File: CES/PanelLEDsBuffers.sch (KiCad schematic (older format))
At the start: 67 parts

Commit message: ExpansionConnectors
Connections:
- net at J?.1 (Pin_1): now also U?.6; no longer U?.12
- net at J?.10 (Pin_10): now also U?.12; no longer U?.6
- net at J?.11 (Pin_11): now also U?.2; no longer U?.4
- net at J?.12 (Pin_12): now also U?.4; no longer U?.2
- net at J?.13 (Pin_13): now also U?.6; no longer U?.12
- net at J?.14 (Pin_14): now also U?.8; no longer U?.10
- net at J?.15 (Pin_15): now also U?.10; no longer U?.8
- net at J?.16 (Pin_16): now also U?.12; no longer U?.6
- net at J?.2 (Pin_2): now also U?.8; no longer U?.10
- net at J?.3 (Pin_3): now also U?.10; no longer U?.8
- net at J?.4 (Pin_4): now also U?.12; no longer U?.6
- net at J?.5 (Pin_5): now also U?.2; no longer U?.4
- net at J?.6 (Pin_6): now also U?.4; no longer U?.2
- net at J?.7 (Pin_7): now also U?.6; no longer U?.12
- net at J?.8 (Pin_8): now also U?.8; no longer U?.10
- net at J?.9 (Pin_9): now also U?.10; no longer U?.8
- net at J?.1 (Pin_1): now also U?.10; no longer U?.4
- net at J?.10 (Pin_10): now also U?.4; no longer U?.10
- net at J?.11 (Pin_11): now also U?.6; no longer U?.8
- net at J?.12 (Pin_12): now also U?.8; no longer U?.6
- net at J?.13 (Pin_13): now also U?.10; no longer U?.4
- net at J?.14 (Pin_14): now also U?.12; no longer U?.2
- net at J?.15 (Pin_15): now also U?.2; no longer U?.12
- net at J?.16 (Pin_16): now also U?.4; no longer U?.10
- net at J?.2 (Pin_2): now also U?.12; no longer U?.2
- net at J?.3 (Pin_3): now also U?.2; no longer U?.12
- net at J?.4 (Pin_4): now also U?.4; no longer U?.10
- net at J?.5 (Pin_5): now also U?.6; no longer U?.8
- net at J?.6 (Pin_6): now also U?.8; no longer U?.6
- net at J?.7 (Pin_7): now also U?.10; no longer U?.4
- net at J?.8 (Pin_8): now also U?.12; no longer U?.2
- net at J?.9 (Pin_9): now also U?.2; no longer U?.12
- net at J?.1 (Pin_1): now also U?.2; no longer U?.8
- net at J?.10 (Pin_10): now also U?.8; no longer U?.2
- net at J?.11 (Pin_11): now also U?.10; no longer U?.12
- net at J?.12 (Pin_12): now also U?.12; no longer U?.10
- net at J?.13 (Pin_13): now also U?.2; no longer U?.8
- net at J?.14 (Pin_14): now also U?.4; no longer U?.6
- net at J?.15 (Pin_15): now also U?.6; no longer U?.4
- net at J?.16 (Pin_16): now also U?.8; no longer U?.2
- net at J?.2 (Pin_2): now also U?.4; no longer U?.6
- net at J?.3 (Pin_3): now also U?.6; no longer U?.4
- net at J?.4 (Pin_4): now also U?.8; no longer U?.2
- net at J?.5 (Pin_5): now also U?.10; no longer U?.12
- net at J?.6 (Pin_6): now also U?.12; no longer U?.10
- net at J?.7 (Pin_7): now also U?.2; no longer U?.8
- net at J?.8 (Pin_8): now also U?.4; no longer U?.6
- net at J?.9 (Pin_9): now also U?.6; no longer U?.4
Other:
- note removed: "TODO: Find a \nbetter connector"
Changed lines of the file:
@@
 $Descr A4 11693 8268
 encoding utf-8
-Sheet 12 15
+Sheet 12 16
 Title "CES"
 Date "2021-04-24"
@@
 L Connector:Conn_01x16_Male J?
 U 1 1 60C2ED9D
-P 9250 3350
+P 9250 3250
 AR Path="/60832DB9/60C2ED9D" Ref="J?"  Part="1"
 AR Path="/60832DB9/60BC5CB5/60C2ED9D" Ref="J?"  Part="1"
-F 0 "J?" H 9350 2400 50  0000 R CNN
-F 1 "PanelEnd" H 9450 4150 50  0000 R CNN
-F 2 "" H 9250 3350 50  0001 C CNN
-F 3 "~" H 9250 3350 50  0001 C CNN
-	1    9250 3350
-	-1   0    0    1
+F 0 "J?" H 9350 2300 50  0000 R CNN
+F 1 "PanelEnd" H 9450 4050 50  0000 R CNN
+F 2 "" H 9250 3250 50  0001 C CNN
+F 3 "~" H 9250 3250 50  0001 C CNN
+	1    9250 3250
+	-1   0    0    -1
 $EndComp
 Wire Wire Line
@@
 L Connector:Conn_01x16_Male J?
 U 1 1 60C2EDF1
-P 6750 3350
+P 6750 3250
 AR Path="/60832DB9/60C2EDF1" Ref="J?"  Part="1"
 AR Path="/60832DB9/60BC5CB5/60C2EDF1" Ref="J?"  Part="1"
-F 0 "J?" H 6850 2400 50  0000 R CNN
-F 1 "PanelMem" H 6950 4150 50  0000 R CNN
-F 2 "" H 6750 3350 50  0001 C CNN
-F 3 "~" H 6750 3350 50  0001 C CNN
-	1    6750 3350
-	-1   0    0    1
+F 0 "J?" H 6850 2300 50  0000 R CNN
+F 1 "PanelMem" H 6950 4050 50  0000 R CNN
+F 2 "" H 6750 3250 50  0001 C CNN
+F 3 "~" H 6750 3250 50  0001 C CNN
+	1    6750 3250
+	-1   0    0    -1
 $EndComp
 Wire Wire Line
@@
 Text GLabel 4950 1150 0    50   Input ~ 0
 VDB1
-Text Notes 9000 4400 0    50   ~ 0
-TODO: Find a \nbetter connector
 Wire Wire Line
 	4950 800  5150 800
@@
 L Connector:Conn_01x16_Male J?
 U 1 1 60C2EE48
-P 4450 3350
+P 4450 3250
 AR Path="/60832DB9/60C2EE48" Ref="J?"  Part="1"
 AR Path="/60832DB9/60BC5CB5/60C2EE48" Ref="J?"  Part="1"
-F 0 "J?" H 4550 2400 50  0000 R CNN
-F 1 "PanelRT" H 4650 4150 50  0000 R CNN
-F 2 "" H 4450 3350 50  0001 C CNN
-F 3 "~" H 4450 3350 50  0001 C CNN
-	1    4450 3350
-	-1   0    0    1
+F 0 "J?" H 4550 2300 50  0000 R CNN
+F 1 "PanelRT" H 4650 4050 50  0000 R CNN
+F 2 "" H 4450 3250 50  0001 C CNN
+F 3 "~" H 4450 3250 50  0001 C CNN
+	1    4450 3250
+	-1   0    0    -1
 $EndComp
 Wire Wire Line

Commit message: Control Unit
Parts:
- gave numbers to parts that had none: 19

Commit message: Assigning footprints and generating netlist
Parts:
- C1301, C1302, C1303, C1304, C1305, C1306, C1307, C1308: footprint (none) -> Capacitor_THT:CP_Radial_D5.0mm_P2.50mm
- J1301, J1302, J1303: footprint (none) -> Connector_PinHeader_2.54mm:PinHeader_1x16_P2.54mm_Vertical
- U1301, U1302, U1303, U1304, U1305, U1306, U1307, U1308: footprint (none) -> Package_DIP:DIP-14_W7.62mm

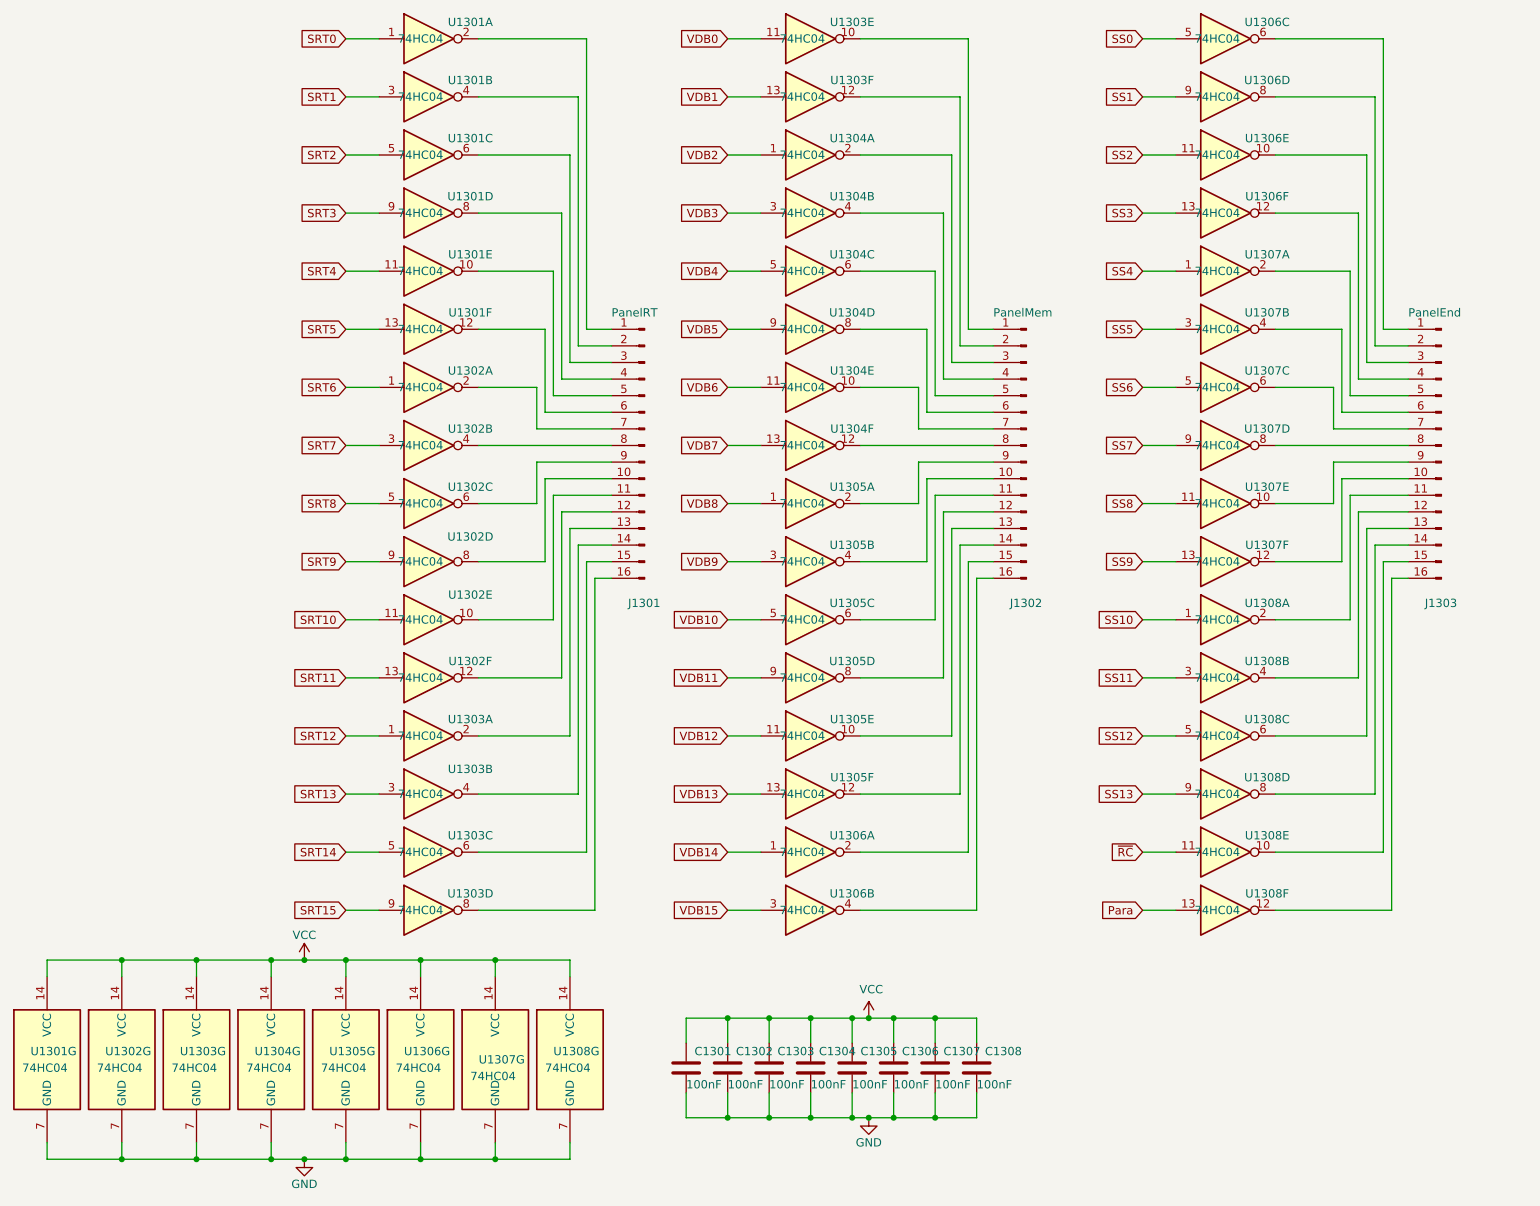
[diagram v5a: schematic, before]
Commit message: Correcting footprints errors
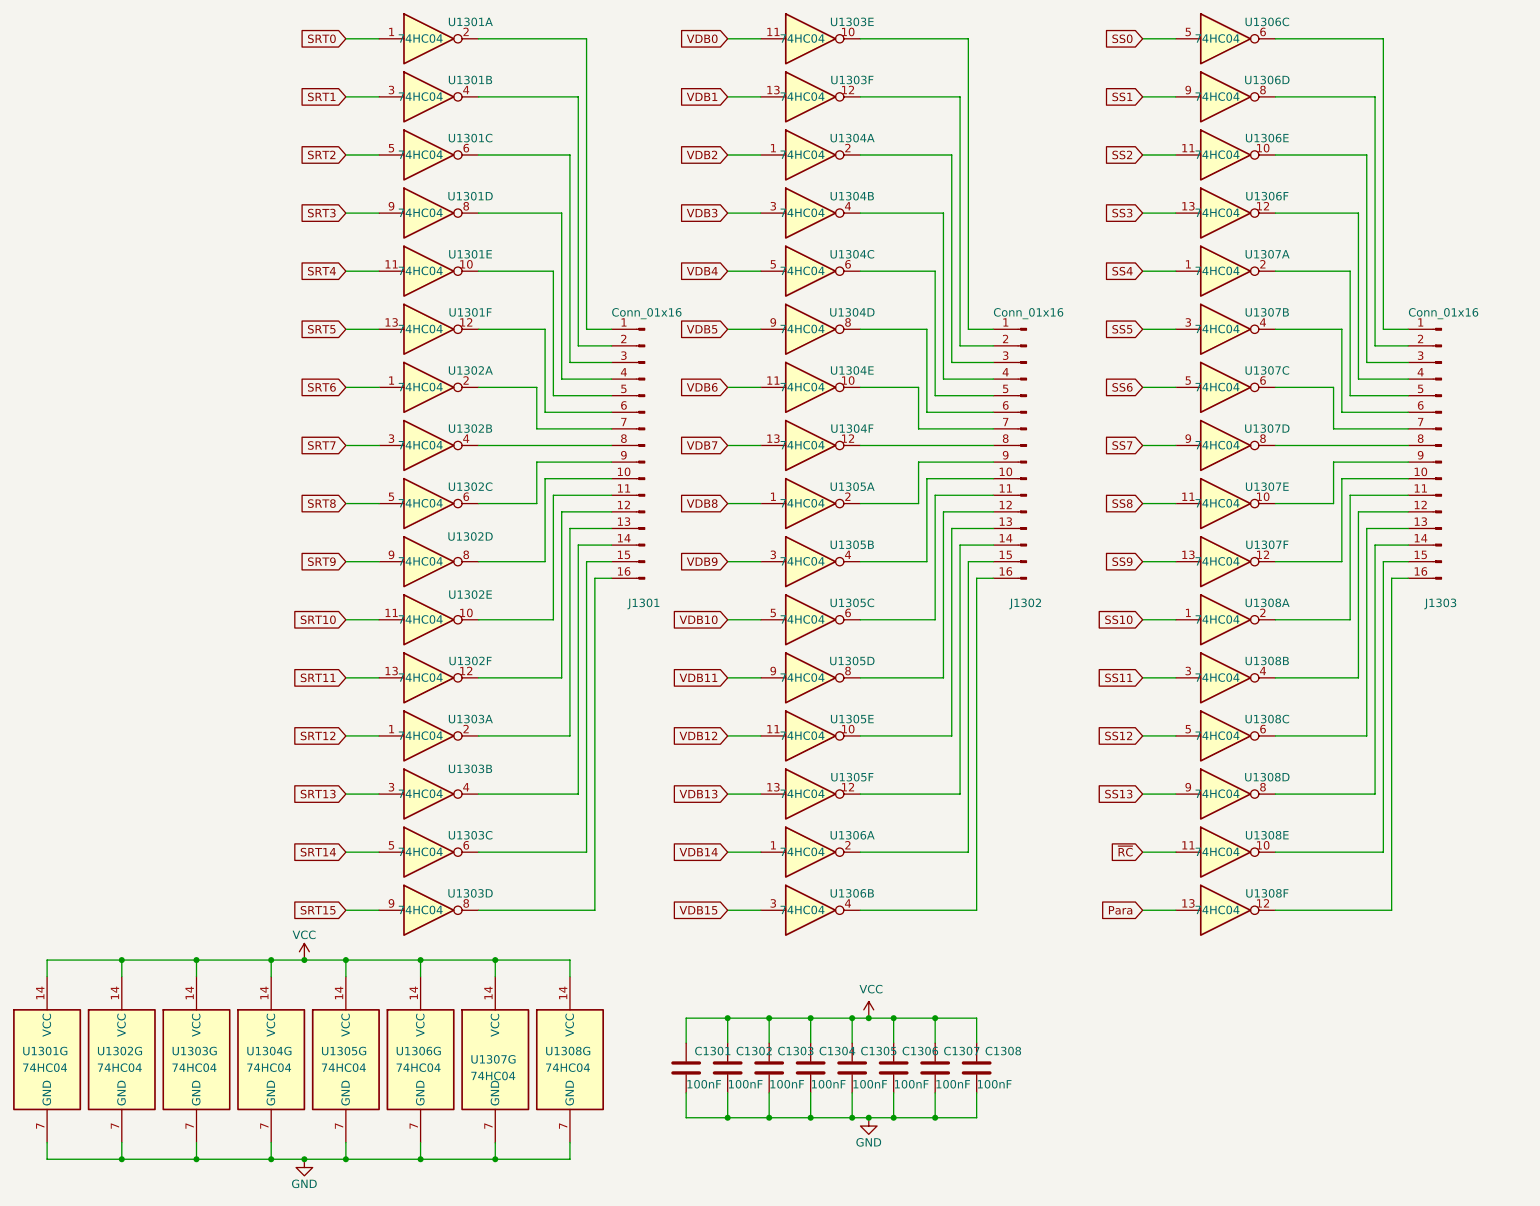
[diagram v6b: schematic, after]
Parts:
- C1301, C1302, C1303, C1304, C1305, C1306, C1307, C1308: footprint Capacitor_THT:CP_Radial_D5.0mm_P2.50mm -> Capacitor_THT:C_Disc_D4.3mm_W1.9mm_P5.00mm
- J1301: value PanelRT -> Conn_01x16
- J1302: value PanelMem -> Conn_01x16
- J1303: value PanelEnd -> Conn_01x16
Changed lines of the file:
@@
 AR Path="/60832DB9/60BC5CB5/60C2ED9D" Ref="J1303"  Part="1"
 F 0 "J1303" H 9350 2300 50  0000 R CNN
-F 1 "PanelEnd" H 9450 4050 50  0000 R CNN
+F 1 "Conn_01x16" H 9450 4050 50  0000 R CNN
 F 2 "Connector_PinHeader_2.54mm:PinHeader_1x16_P2.54mm_Vertical" H 9250 3250 50  0001 C CNN
 F 3 "~" H 9250 3250 50  0001 C CNN
@@
 AR Path="/60832DB9/60BC5CB5/60C2EDF1" Ref="J1302"  Part="1"
 F 0 "J1302" H 6850 2300 50  0000 R CNN
-F 1 "PanelMem" H 6950 4050 50  0000 R CNN
+F 1 "Conn_01x16" H 6950 4050 50  0000 R CNN
 F 2 "Connector_PinHeader_2.54mm:PinHeader_1x16_P2.54mm_Vertical" H 6750 3250 50  0001 C CNN
 F 3 "~" H 6750 3250 50  0001 C CNN
@@
 AR Path="/60832DB9/60BC5CB5/60C2EE48" Ref="J1301"  Part="1"
 F 0 "J1301" H 4550 2300 50  0000 R CNN
-F 1 "PanelRT" H 4650 4050 50  0000 R CNN
+F 1 "Conn_01x16" H 4650 4050 50  0000 R CNN
 F 2 "Connector_PinHeader_2.54mm:PinHeader_1x16_P2.54mm_Vertical" H 4450 3250 50  0001 C CNN
 F 3 "~" H 4450 3250 50  0001 C CNN
@@
 U 7 1 60CD4AAA
 P 2650 6950
-F 0 "U1305" H 2550 7000 50  0000 L CNN
+F 0 "U1305" H 2500 7000 50  0000 L CNN
 F 1 "74HC04" H 2500 6900 50  0000 L CNN
 F 2 "Package_DIP:DIP-14_W7.62mm" H 2650 6950 50  0001 C CNN
@@
 U 7 1 60CD4AB0
 P 3100 6950
-F 0 "U1306" H 3000 7000 50  0000 L CNN
+F 0 "U1306" H 2950 7000 50  0000 L CNN
 F 1 "74HC04" H 2950 6900 50  0000 L CNN
 F 2 "Package_DIP:DIP-14_W7.62mm" H 3100 6950 50  0001 C CNN
@@
 U 7 1 60CD4AB6
 P 3550 6950
-F 0 "U1307" H 3450 6950 50  0000 L CNN
+F 0 "U1307" H 3400 6950 50  0000 L CNN
 F 1 "74HC04" H 3400 6850 50  0000 L CNN
 F 2 "Package_DIP:DIP-14_W7.62mm" H 3550 6950 50  0001 C CNN
@@
 U 7 1 60CD4ABC
 P 4000 6950
-F 0 "U1308" H 3900 7000 50  0000 L CNN
+F 0 "U1308" H 3850 7000 50  0000 L CNN
 F 1 "74HC04" H 3850 6900 50  0000 L CNN
 F 2 "Package_DIP:DIP-14_W7.62mm" H 4000 6950 50  0001 C CNN
@@
 U 7 1 60CD4AC2
 P 850 6950
-F 0 "U1301" H 750 7000 50  0000 L CNN
+F 0 "U1301" H 700 7000 50  0000 L CNN
 F 1 "74HC04" H 700 6900 50  0000 L CNN
 F 2 "Package_DIP:DIP-14_W7.62mm" H 850 6950 50  0001 C CNN
@@
 U 7 1 60CD4AC8
 P 1300 6950
-F 0 "U1302" H 1200 7000 50  0000 L CNN
+F 0 "U1302" H 1150 7000 50  0000 L CNN
 F 1 "74HC04" H 1150 6900 50  0000 L CNN
 F 2 "Package_DIP:DIP-14_W7.62mm" H 1300 6950 50  0001 C CNN
@@
 U 7 1 60CD4ACE
 P 1750 6950
-F 0 "U1303" H 1650 7000 50  0000 L CNN
+F 0 "U1303" H 1600 7000 50  0000 L CNN
 F 1 "74HC04" H 1600 6900 50  0000 L CNN
 F 2 "Package_DIP:DIP-14_W7.62mm" H 1750 6950 50  0001 C CNN
@@
 U 7 1 60CD4AD4
 P 2200 6950
-F 0 "U1304" H 2100 7000 50  0000 L CNN
+F 0 "U1304" H 2050 7000 50  0000 L CNN
 F 1 "74HC04" H 2050 6900 50  0000 L CNN
 F 2 "Package_DIP:DIP-14_W7.62mm" H 2200 6950 50  0001 C CNN
@@
 F 0 "C1307" H 6250 7100 50  0000 L CNN
 F 1 "100nF" H 6200 6900 50  0000 L CNN
-F 2 "Capacitor_THT:CP_Radial_D5.0mm_P2.50mm" H 6238 6850 50  0001 C CNN
+F 2 "Capacitor_THT:C_Disc_D4.3mm_W1.9mm_P5.00mm" H 6238 6850 50  0001 C CNN
 F 3 "~" H 6200 7000 50  0001 C CNN
 	1    6200 7000
@@
 F 0 "C1308" H 6500 7100 50  0000 L CNN
 F 1 "100nF" H 6450 6900 50  0000 L CNN
-F 2 "Capacitor_THT:CP_Radial_D5.0mm_P2.50mm" H 6488 6850 50  0001 C CNN
+F 2 "Capacitor_THT:C_Disc_D4.3mm_W1.9mm_P5.00mm" H 6488 6850 50  0001 C CNN
 F 3 "~" H 6450 7000 50  0001 C CNN
 	1    6450 7000
@@
 F 0 "C1306" H 6000 7100 50  0000 L CNN
 F 1 "100nF" H 5950 6900 50  0000 L CNN
-F 2 "Capacitor_THT:CP_Radial_D5.0mm_P2.50mm" H 5988 6850 50  0001 C CNN
+F 2 "Capacitor_THT:C_Disc_D4.3mm_W1.9mm_P5.00mm" H 5988 6850 50  0001 C CNN
 F 3 "~" H 5950 7000 50  0001 C CNN
 	1    5950 7000
@@
 F 0 "C1305" H 5750 7100 50  0000 L CNN
 F 1 "100nF" H 5700 6900 50  0000 L CNN
-F 2 "Capacitor_THT:CP_Radial_D5.0mm_P2.50mm" H 5738 6850 50  0001 C CNN
+F 2 "Capacitor_THT:C_Disc_D4.3mm_W1.9mm_P5.00mm" H 5738 6850 50  0001 C CNN
 F 3 "~" H 5700 7000 50  0001 C CNN
 	1    5700 7000
@@
 F 0 "C1304" H 5500 7100 50  0000 L CNN
 F 1 "100nF" H 5450 6900 50  0000 L CNN
-F 2 "Capacitor_THT:CP_Radial_D5.0mm_P2.50mm" H 5488 6850 50  0001 C CNN
+F 2 "Capacitor_THT:C_Disc_D4.3mm_W1.9mm_P5.00mm" H 5488 6850 50  0001 C CNN
 F 3 "~" H 5450 7000 50  0001 C CNN
 	1    5450 7000
@@
 F 0 "C1303" H 5250 7100 50  0000 L CNN
 F 1 "100nF" H 5200 6900 50  0000 L CNN
-F 2 "Capacitor_THT:CP_Radial_D5.0mm_P2.50mm" H 5238 6850 50  0001 C CNN
+F 2 "Capacitor_THT:C_Disc_D4.3mm_W1.9mm_P5.00mm" H 5238 6850 50  0001 C CNN
 F 3 "~" H 5200 7000 50  0001 C CNN
 	1    5200 7000
@@
 F 0 "C1302" H 5000 7100 50  0000 L CNN
 F 1 "100nF" H 4950 6900 50  0000 L CNN
-F 2 "Capacitor_THT:CP_Radial_D5.0mm_P2.50mm" H 4988 6850 50  0001 C CNN
+F 2 "Capacitor_THT:C_Disc_D4.3mm_W1.9mm_P5.00mm" H 4988 6850 50  0001 C CNN
 F 3 "~" H 4950 7000 50  0001 C CNN
 	1    4950 7000
@@
 F 0 "C1301" H 4750 7100 50  0000 L CNN
 F 1 "100nF" H 4700 6900 50  0000 L CNN
-F 2 "Capacitor_THT:CP_Radial_D5.0mm_P2.50mm" H 4738 6850 50  0001 C CNN
+F 2 "Capacitor_THT:C_Disc_D4.3mm_W1.9mm_P5.00mm" H 4738 6850 50  0001 C CNN
 F 3 "~" H 4700 7000 50  0001 C CNN
 	1    4700 7000
